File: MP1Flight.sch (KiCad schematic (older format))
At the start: 19 parts, among them SW1 SW_Push, U2 VisionSOM-STM32MP1

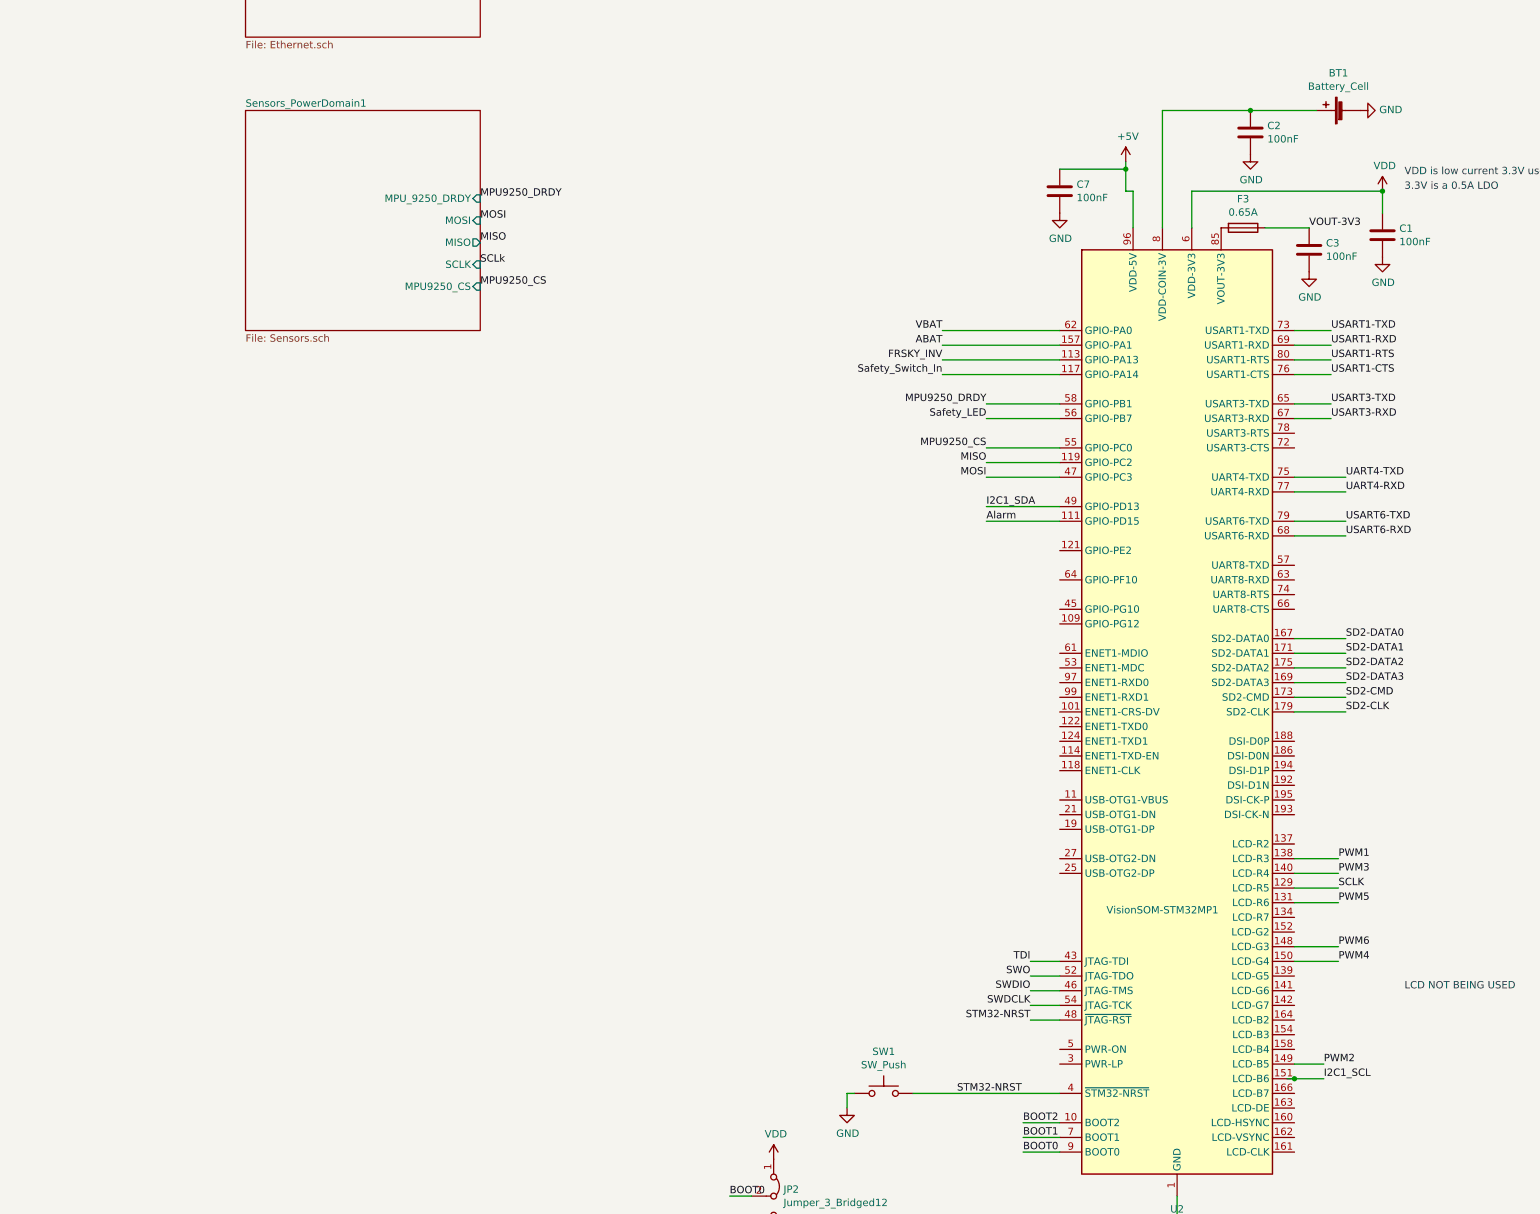
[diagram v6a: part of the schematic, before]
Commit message: Wired up IMUs signals
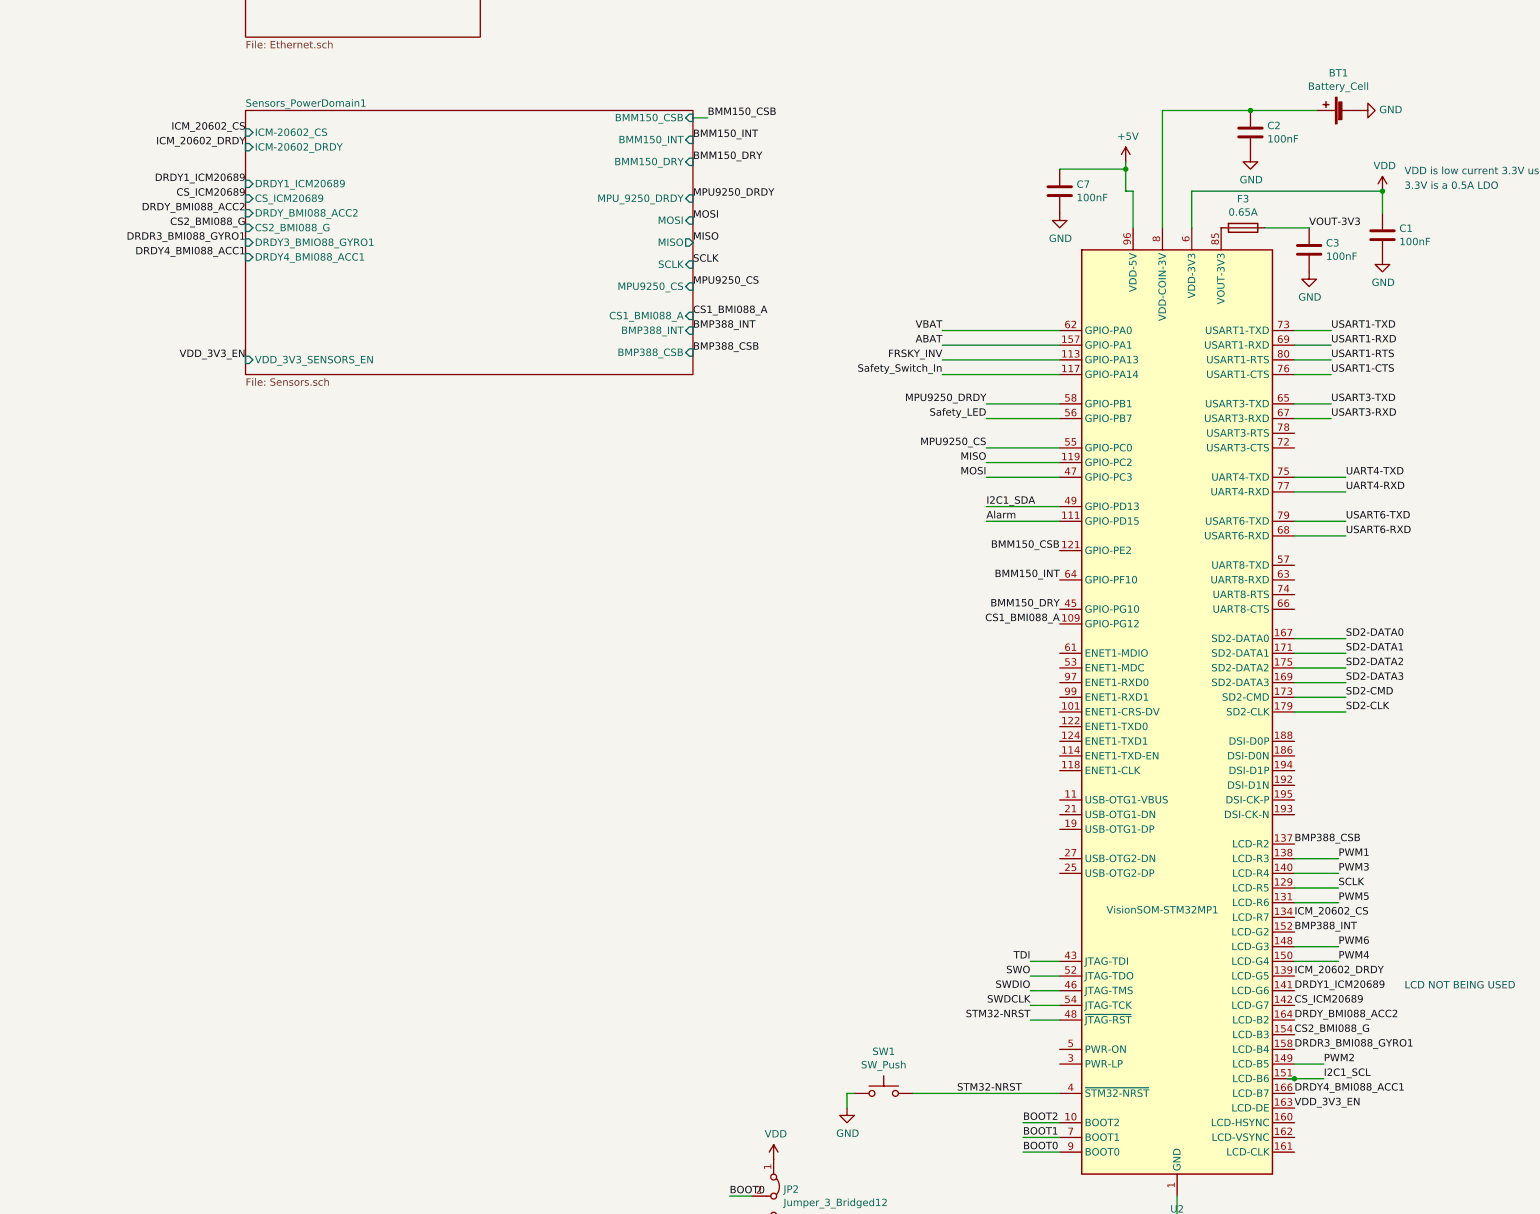
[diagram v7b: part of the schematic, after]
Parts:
- C19: footprint (none) -> Capacitor_SMD:C_0603_1608Metric_Pad1.05x0.95mm_HandSolder
- R2, R5: footprint (none) -> Resistor_SMD:R_0603_1608Metric_Pad1.05x0.95mm_HandSolder
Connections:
- net labels added: BMM150_CSB, BMM150_DRY, BMM150_INT, BMP388_CSB, BMP388_INT, CS1_BMI088_A, CS2_BMI088_G, CS_ICM20689, DRDR3_BMI088_GYRO1, DRDY1_ICM20689, DRDY4_BMI088_ACC1, DRDY_BMI088_ACC2, ICM_20602_CS, ICM_20602_DRDY, VDD_3V3_EN
- net labels removed: SCLk
- wire segments 108 -> 109
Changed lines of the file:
@@
 F 0 "R5" H 4570 2696 50  0000 L CNN
 F 1 "1M" H 4570 2605 50  0000 L CNN
-F 2 "" V 4430 2650 50  0001 C CNN
+F 2 "Resistor_SMD:R_0603_1608Metric_Pad1.05x0.95mm_HandSolder" V 4430 2650 50  0001 C CNN
 F 3 "~" H 4500 2650 50  0001 C CNN
 	1    4500 2650
@@
 F 0 "R2" H 4520 4096 50  0000 L CNN
 F 1 "1M" H 4520 4005 50  0000 L CNN
-F 2 "" V 4380 4050 50  0001 C CNN
+F 2 "Resistor_SMD:R_0603_1608Metric_Pad1.05x0.95mm_HandSolder" V 4380 4050 50  0001 C CNN
 F 3 "~" H 4450 4050 50  0001 C CNN
 	1    4450 4050
@@
 F 0 "C19" H 4700 3950 50  0000 L CNN
 F 1 "100nF" H 4700 4050 50  0000 L CNN
-F 2 "" H 4738 4000 50  0001 C CNN
+F 2 "Capacitor_SMD:C_0603_1608Metric_Pad1.05x0.95mm_HandSolder" H 4738 4000 50  0001 C CNN
 F 3 "~" H 4700 4150 50  0001 C CNN
 	1    4700 4150
@@
 $EndSheet
 $Sheet
-S 7600 3750 1600 1500
+S 7600 3750 3050 1800
 U 5F064FD4
 F0 "Sensors_PowerDomain1" 50
 F1 "Sensors.sch" 50
-F2 "MPU_9250_DRDY" I R 9200 4350 50
-F3 "MOSI" I R 9200 4500 50
-F4 "MISO" O R 9200 4650 50
-F5 "SCLK" I R 9200 4800 50
-F6 "MPU9250_CS" I R 9200 4950 50
+F2 "MPU_9250_DRDY" I R 10650 4350 50
+F3 "MOSI" I R 10650 4500 50
+F4 "MISO" O R 10650 4650 50
+F5 "SCLK" I R 10650 4800 50
+F6 "MPU9250_CS" I R 10650 4950 50
+F7 "ICM-20602_CS" I L 7600 3900 50
+F8 "VDD_3V3_SENSORS_EN" I L 7600 5450 50
+F9 "ICM-20602_DRDY" I L 7600 4000 50
+F10 "DRDY1_ICM20689" I L 7600 4250 50
+F11 "CS_ICM20689" I L 7600 4350 50
+F12 "DRDY_BMI088_ACC2" I L 7600 4450 50
+F13 "CS2_BMI088_G" I L 7600 4550 50
+F14 "DRDY3_BMIO88_GYRO1" I L 7600 4650 50
+F15 "DRDY4_BMI088_ACC1" I L 7600 4750 50
+F16 "CS1_BMI088_A" I R 10650 5150 50
+F17 "BMM150_DRY" I R 10650 4100 50
+F18 "BMM150_INT" I R 10650 3950 50
+F19 "BMM150_CSB" I R 10650 3800 50
+F20 "BMP388_CSB" I R 10650 5400 50
+F21 "BMP388_INT" I R 10650 5250 50
 $EndSheet
 $Comp
@@
 Wire Wire Line
 	14550 4550 14850 4550
-Text Label 9200 4350 0    50   ~ 0
+Text Label 10650 4350 0    50   ~ 0
 MPU9250_DRDY
-Text Label 9200 4500 0    50   ~ 0
+Text Label 10650 4500 0    50   ~ 0
 MOSI
-Text Label 9200 4650 0    50   ~ 0
+Text Label 10650 4650 0    50   ~ 0
 MISO
-Text Label 9200 4800 0    50   ~ 0
-SCLk
-Text Label 9200 4950 0    50   ~ 0
+Text Label 10650 4800 0    50   ~ 0
+SCLK
+Text Label 10650 4950 0    50   ~ 0
 MPU9250_CS
 Wire Wire Line
@@
 F1 "Ethernet.sch" 50
 $EndSheet
+Wire Wire Line
+	10750 3800 10650 3800
+Text Label 10750 3800 0    50   ~ 0
+BMM150_CSB
+Text Label 13150 6750 2    50   ~ 0
+BMM150_CSB
+Text Label 13150 6950 2    50   ~ 0
+BMM150_INT
+Text Label 10650 3950 0    50   ~ 0
+BMM150_INT
+Text Label 10650 4100 0    50   ~ 0
+BMM150_DRY
+Text Label 13150 7150 2    50   ~ 0
+BMM150_DRY
+Text Label 13150 7250 2    50   ~ 0
+CS1_BMI088_A
+Text Label 10650 5150 0    50   ~ 0
+CS1_BMI088_A
+Text Label 10650 5400 0    50   ~ 0
+BMP388_CSB
+Text Label 14750 8750 0    50   ~ 0
+BMP388_CSB
+Text Label 7600 3900 2    50   ~ 0
+ICM_20602_CS
+Text Label 14750 9250 0    50   ~ 0
+ICM_20602_CS
+Text Label 10650 5250 0    50   ~ 0
+BMP388_INT
+Text Label 14750 9350 0    50   ~ 0
+BMP388_INT
+Text Label 7600 4000 2    50   ~ 0
+ICM_20602_DRDY
+Text Label 14750 9650 0    50   ~ 0
+ICM_20602_DRDY
+Text Label 7600 4250 2    50   ~ 0
+DRDY1_ICM20689
+Text Label 14750 9750 0    50   ~ 0
+DRDY1_ICM20689
+Text Label 7600 4350 2    50   ~ 0
+CS_ICM20689
+Text Label 7600 4450 2    50   ~ 0
+DRDY_BMI088_ACC2
+Text Label 14750 9850 0    50   ~ 0
+CS_ICM20689
+Text Label 14750 9950 0    50   ~ 0
+DRDY_BMI088_ACC2
+Text Label 7600 4550 2    50   ~ 0
+CS2_BMI088_G
+Text Label 14750 10050 0    50   ~ 0
+CS2_BMI088_G
+Text Label 7600 4650 2    50   ~ 0
+DRDR3_BMI088_GYRO1
+Text Label 7600 4750 2    50   ~ 0
+DRDY4_BMI088_ACC1
+Text Label 14750 10150 0    50   ~ 0
+DRDR3_BMI088_GYRO1
+Text Label 14750 10450 0    50   ~ 0
+DRDY4_BMI088_ACC1
+Text Label 14750 10550 0    50   ~ 0
+VDD_3V3_EN
+Text Label 7600 5450 2    50   ~ 0
+VDD_3V3_EN
 $EndSCHEMATC
